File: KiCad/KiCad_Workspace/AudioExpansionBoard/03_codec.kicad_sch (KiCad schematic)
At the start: 22 parts, among them U1 XTAC5212IRGER, U3 IM67D128B, U4 IM67D128B

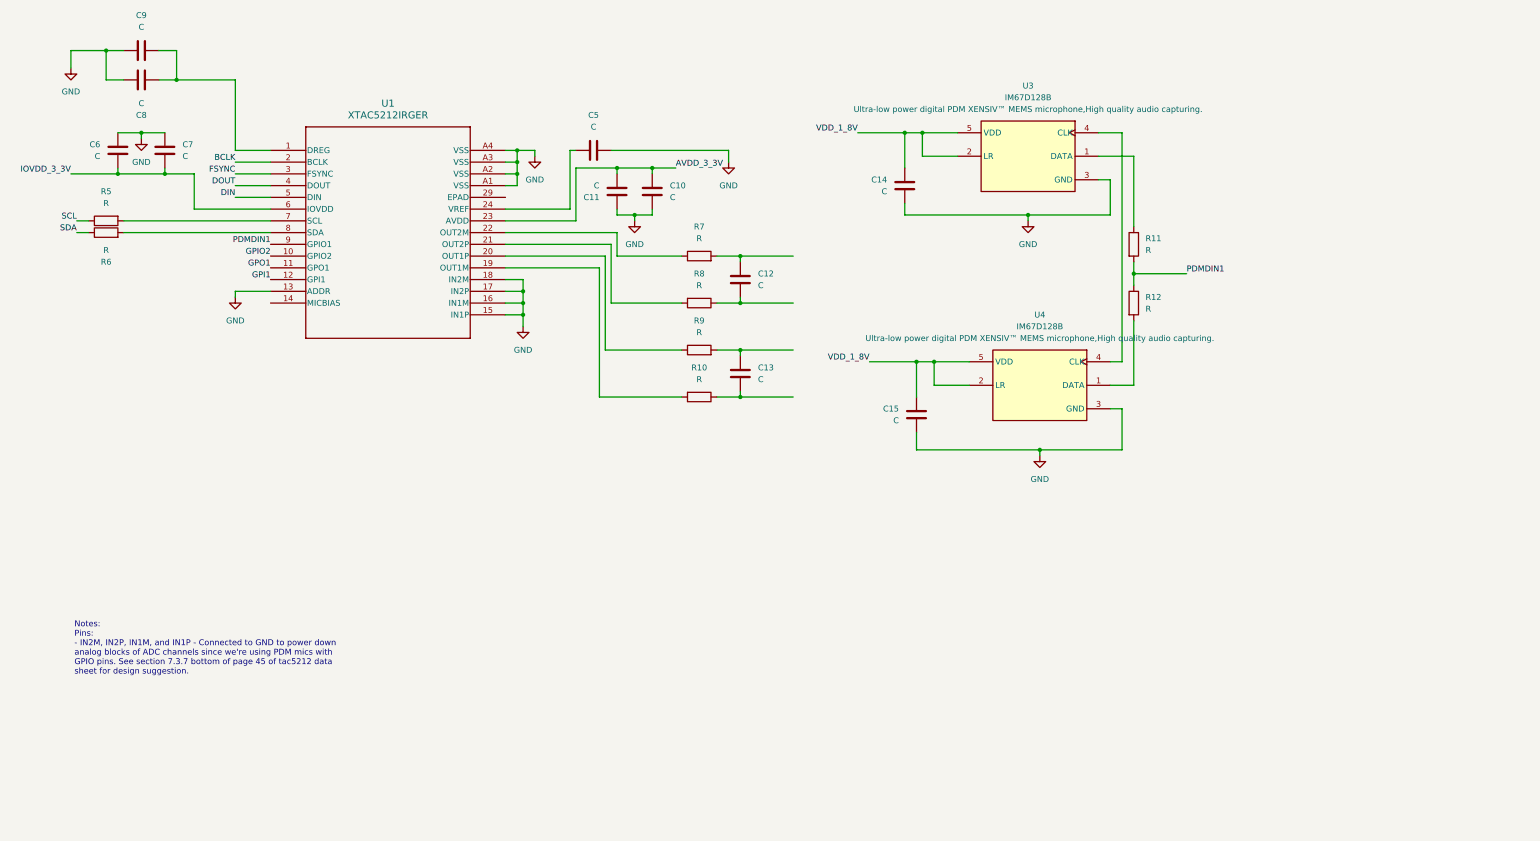
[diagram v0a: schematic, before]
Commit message: Codec sch update and project folder organization
Defined most component values for codec schematic as per ti-tac5212 codec datasheet and reorganized folder and file structure of project
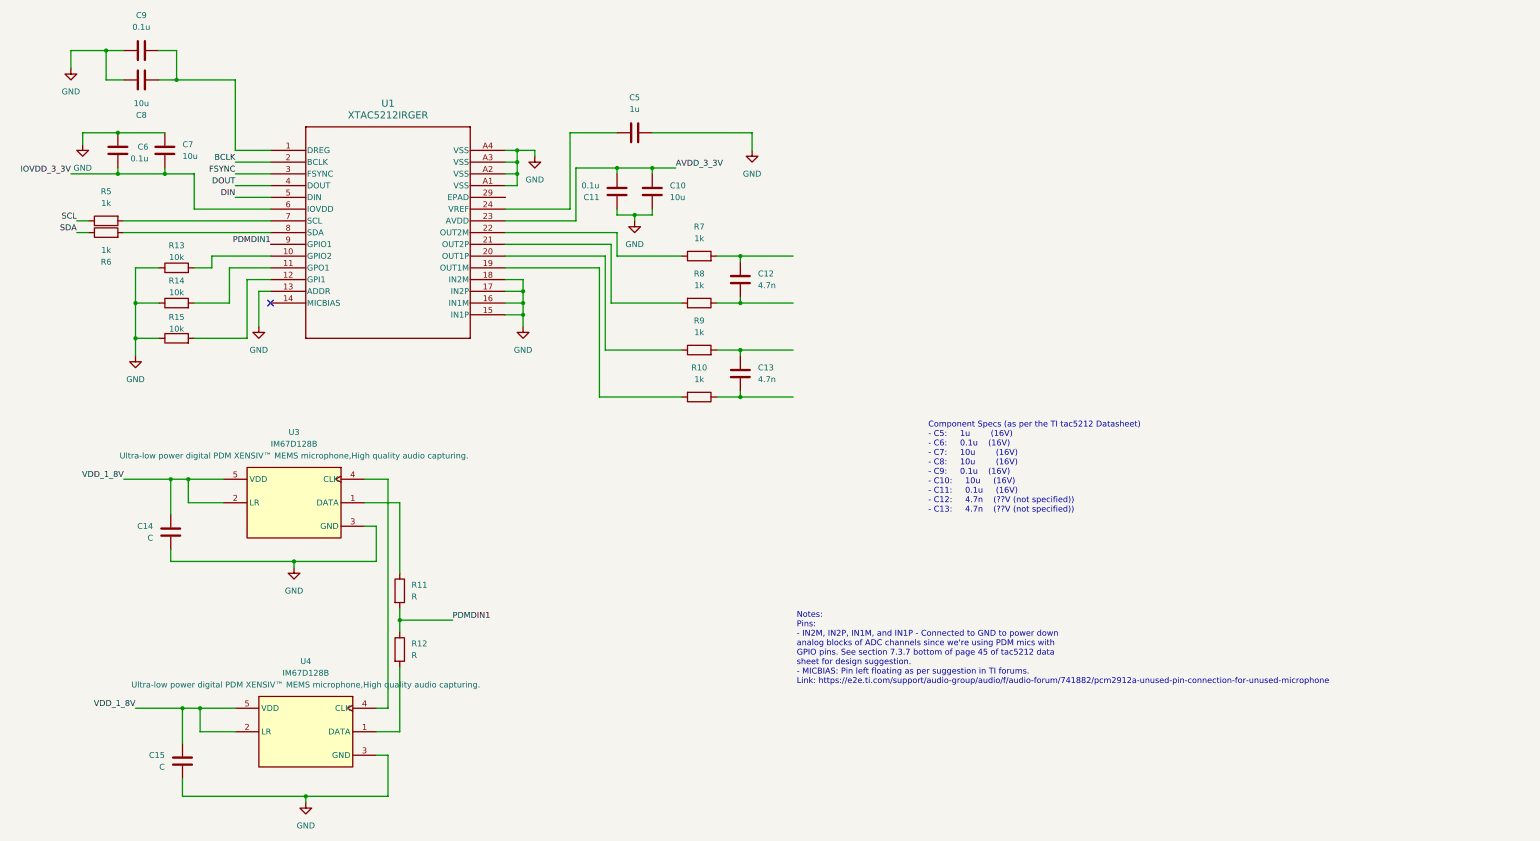
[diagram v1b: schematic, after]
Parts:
- added R13, R14, R15: 10k, symbol Device:R
- C10, C7, C8: value C -> 10u
- C11, C6, C9: value C -> 0.1u
- C12, C13: value C -> 4.7n
- C5: value C -> 1u
- R10, R5, R6, R7, R8, R9: value R -> 1k
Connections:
- net GND: now also R13.1, R14.1, R15.1
- net GPI1: no longer names the net of U1.12 (GPI1)
- net GPI1: now also R15.2
- net GPIO2: no longer names the net of U1.10 (GPIO2)
- net GPIO2: now also R13.2
- net GPO1: no longer names the net of U1.11 (GPO1)
- net GPO1: now also R14.2
- no-connect marks 0 -> 1
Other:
- note added: "Component Specs (as per the TI tac5212 Datasheet) - C5: 1u (16V) - C6: 0.1u (16V) - C7: 10u (16V) - C8: 10u (16V) - C9: 0.1u (16V) - C10: 10u (16V) - C11: 0.1u (16V) - C12: 4.7n (??V (not specified)) - C13: 4.7n (??V (not specified))"
- note added: "Notes: Pins: - IN2M, IN2P, IN1M, and IN1P - Connected to GND to power down analog blocks of ADC channels since we're using PDM mics with GPIO pins. See section 7.3.7 bottom of page 45 of tac5212 data sheet for design suggestion. - MICBIAS: Pin left floating as per suggestion in TI forums. Link: https://e2e.ti.com/support/audio-group/audio/f/audio-forum/741882/pcm2912a-unused-pin-connection-for-un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"
- note removed: "Notes: Pins: - IN2M, IN2P, IN1M, and IN1P - Connected to GND to power down analog blocks of ADC channels since we're using PDM mics with GPIO pins. See section 7.3.7 bottom of page 45 of tac5212 data sheet for design suggestion."
- moved on the sheet: C14, C15, C5, R11, R12, U3, U4
